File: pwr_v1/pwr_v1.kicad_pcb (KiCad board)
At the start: 4 copper layers, 166 x 166 mm, 185 parts, among them CN11 Conn_02x36_Odd_Even, CN12 Conn_02x36_Odd_Even, J1 Conn_01x12_Pin, M1 Conn_01x08_Socket, M2 Conn_01x08_Socket, M3 Conn_01x08_Socket, M4 Conn_01x08_Socket, M5 Conn_01x08_Socket, Q1 BSS84, U1 LM2576S-5, U2 LM2576S-12, U3 LM2576S-3.3, U4 LSM6DSLTR

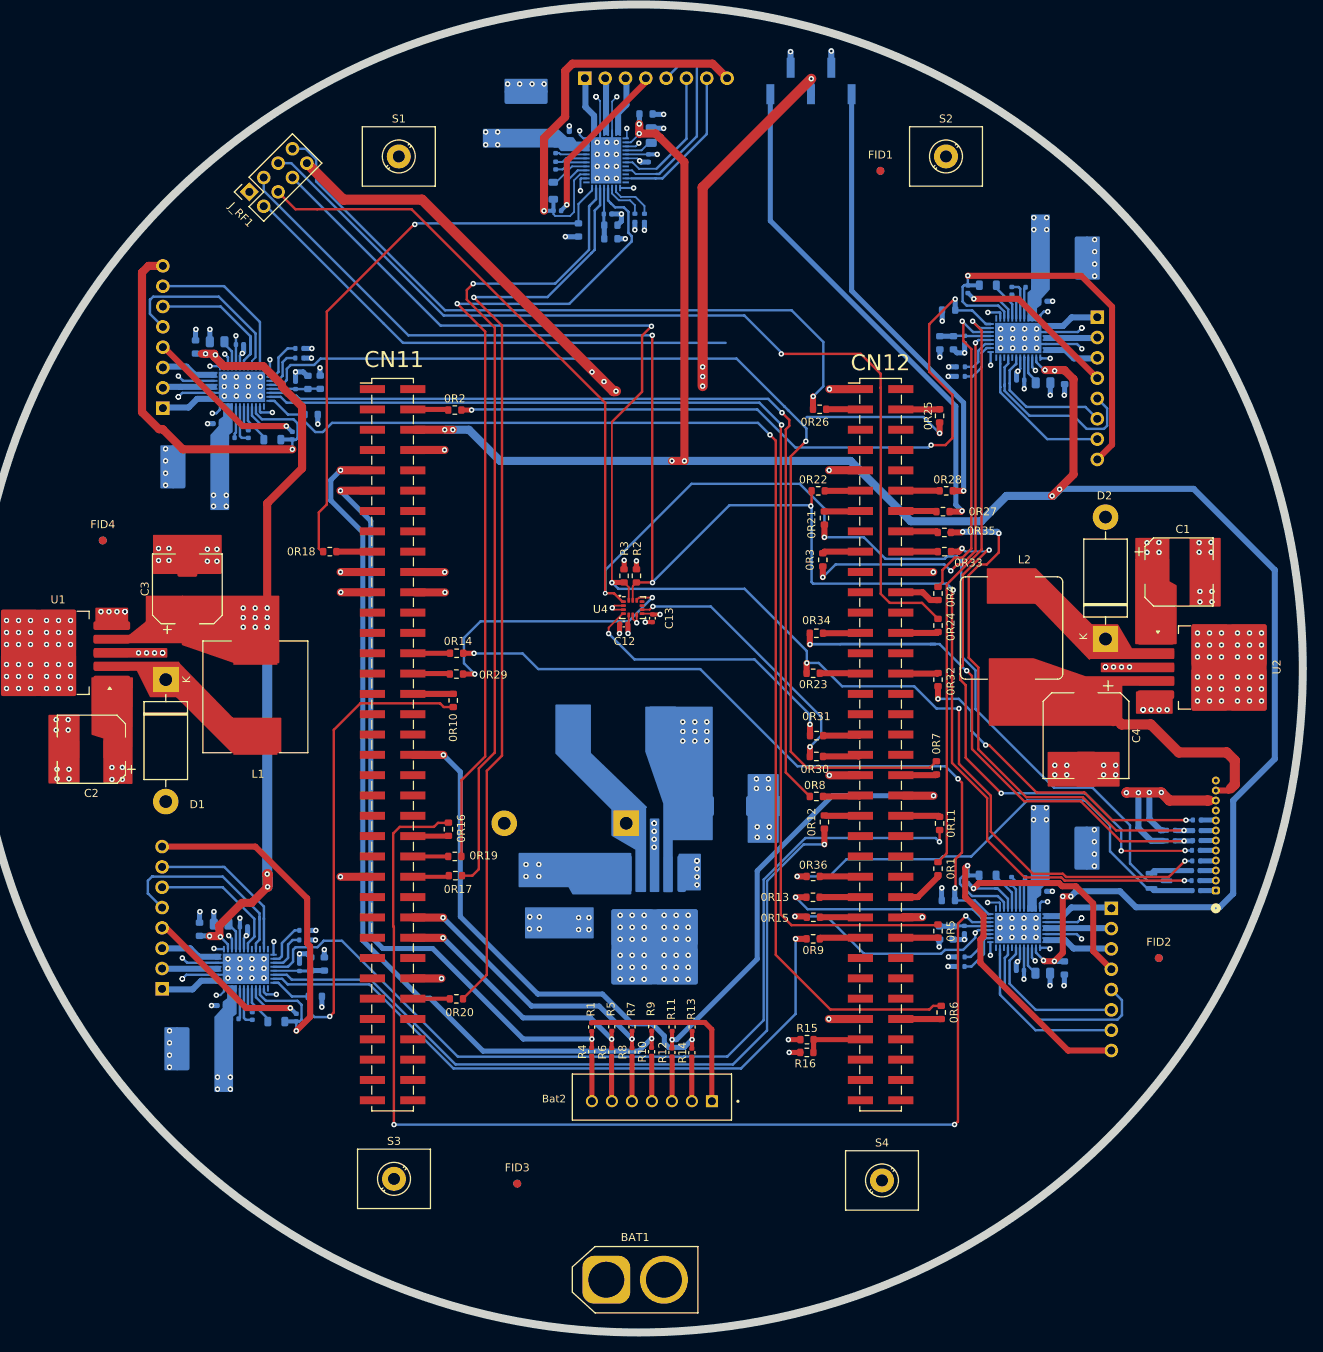
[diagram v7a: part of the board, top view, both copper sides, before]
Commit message: Sch: 0ohm res added to SPI pins, MD footprints updated; Lay: Silkscreen aligned, logo added, DRC
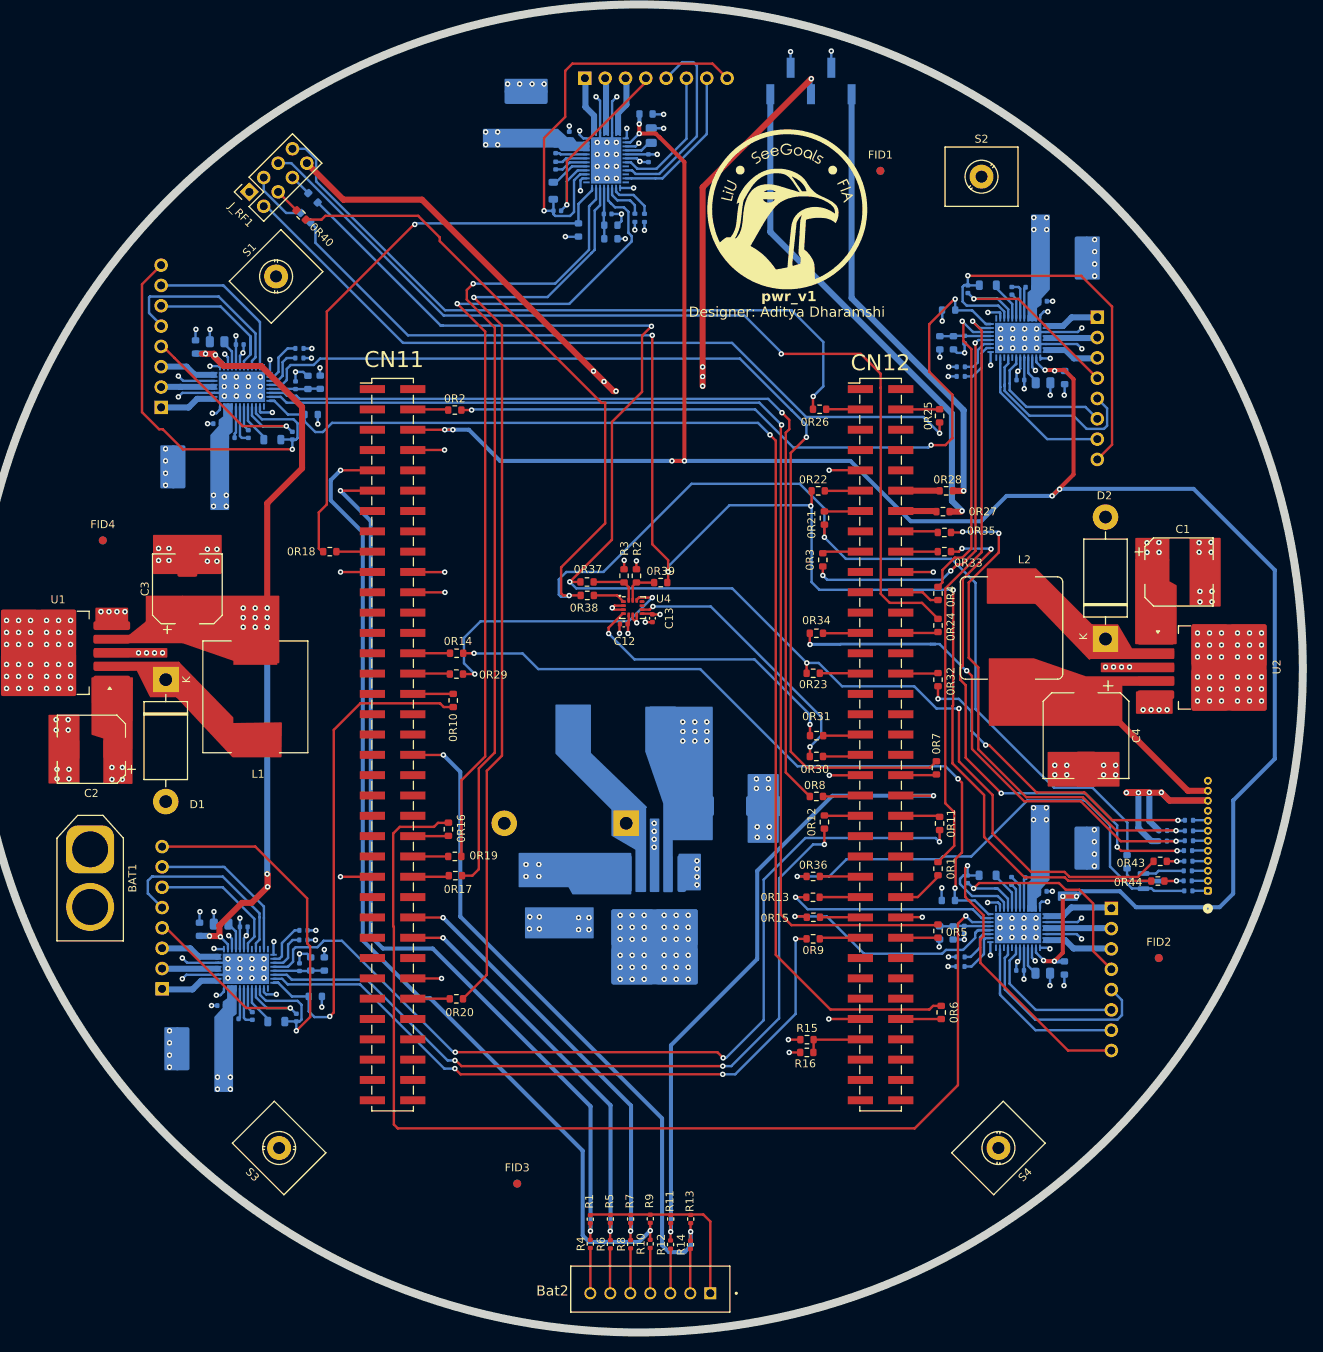
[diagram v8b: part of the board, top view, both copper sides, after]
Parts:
- added 0R37: 0, Resistor_SMD:R_0603_1608Metric, F.Cu at (143.5, 89.2)
- added 0R38: 0, Resistor_SMD:R_0603_1608Metric, F.Cu at (143.6, 90.9)
- added 0R39: 0, Resistor_SMD:R_0603_1608Metric, F.Cu at (152.7, 89.3)
- added 0R40: 0, Resistor_SMD:R_0603_1608Metric, F.Cu at (107.8, 43.3)
- added 0R41: 0, Resistor_SMD:R_0603_1608Metric, B.Cu at (108.3, 43.6)
- added 0R42: 0, Resistor_SMD:R_0603_1608Metric, B.Cu at (109.3, 41.2)
- added 0R43: 0, Resistor_SMD:R_0603_1608Metric, F.Cu at (215.2, 124.1)
- added 0R44: 0, Resistor_SMD:R_0603_1608Metric, F.Cu at (214.9, 126.6)
- added 0R45: 0, Resistor_SMD:R_0603_1608Metric, B.Cu at (211.0, 124.2)
- added G***: LOGO, LOGO, F.Cu at (168.6, 42.6)
- added G***: LOGO, LOGO, B.Cu at (80.6, 81.1)
- 1U1, 2U1, 3U1, 4U1, 5U1: footprint MTR:RGF0040E-IPC_B -> motorDriver:RGF0040E-IPC_B
- moved BAT1 84.0 mm to (81.4, 122.6), turned to -90 degrees
- moved R12 24.0 mm to (154.0, 172.0)
- moved R4 24.0 mm to (143.9, 171.9)
- moved R1 24.0 mm to (143.9, 168.8)
- moved R5 24.0 mm to (146.4, 168.8)
- moved R7 24.0 mm to (149.0, 168.8)
- moved R8 24.0 mm to (149.0, 172.0)
- moved R11 24.0 mm to (154.0, 168.8)
- moved R13 24.0 mm to (156.5, 168.8)
- moved R14 24.0 mm to (156.5, 172.0)
- moved R9 24.0 mm to (151.4, 168.8)
- moved R10 24.0 mm to (151.4, 171.9)
- moved R6 24.0 mm to (146.4, 172.0)
- moved Bat2 24.0 mm to (151.4, 177.6)
- moved S1 21.5 mm to (104.7, 51.0), turned to 45 degrees
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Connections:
- J_RF1 pad 3: /SCK -> /RF/SCK
- J_RF1 pad 4: /MISO -> /RF/MISO
- J_RF1 pad 6: /MOSI -> /RF/MOSI
- Q1 pad 3: /MISO -> /KB/MISO
- R2 pad 2: /SCK -> /IMU/SCL
- R3 pad 2: /MOSI -> /IMU/SDA
- RK2 pad 2: /SCK -> /KB/CLK
- RK4 pad 2: /MOSI -> /KB/MOSI
- U4 pad 1: /MISO -> /IMU/SDO/SA0
- U4 pad 13: /SCK -> /IMU/SCL
- U4 pad 14: /MOSI -> /IMU/SDA
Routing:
- net /Battery Supervisor/O5: track 57.6 -> 81.4 mm
- net /Battery Supervisor/O6: track 63.6 -> 84.5 mm
- net /Battery Supervisor/O2: track 32.2 -> 51.2 mm
- net /Battery Supervisor/O3: track 35.7 -> 54.8 mm
- net /Battery Supervisor/O1: track 96.1 -> 115.0 mm
- net /SCK: track 207.1 -> 188.3 mm, vias 5 -> 4
- net /Battery Supervisor/O4: track 109.2 -> 125.1 mm
- net /RF/CE: track 83.7 -> 97.6 mm
- net 12V: track 34.0 -> 20.9 mm
- net /RF/SCK: track 0.00 -> 7.44 mm
- net /IMU/SDA: track 0.00 -> 6.30 mm
- net /MOSI: track 188.1 -> 183.0 mm, vias 5 -> 4
- net /KB/MISO: track 0.00 -> 5.07 mm
- net /IMU/SCL: track 0.00 -> 4.65 mm
- net /IMU/SDO/SA0: track 0.00 -> 4.14 mm
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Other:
- board text added: "Designer: Aditya Dharamshi"
- board text added: "pwr_v1"
